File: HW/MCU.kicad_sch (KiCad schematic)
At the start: 44 parts, among them J4 UPDI Debug Connector, SW1 Reset, U2 ATmega4809-A, U4 24AA256UID

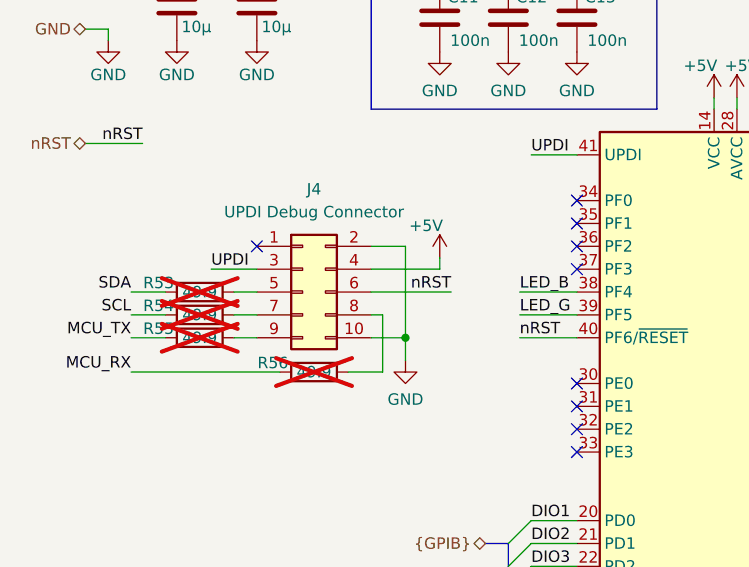
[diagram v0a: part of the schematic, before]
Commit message: Added uart and i2c to jtag connector, docs added
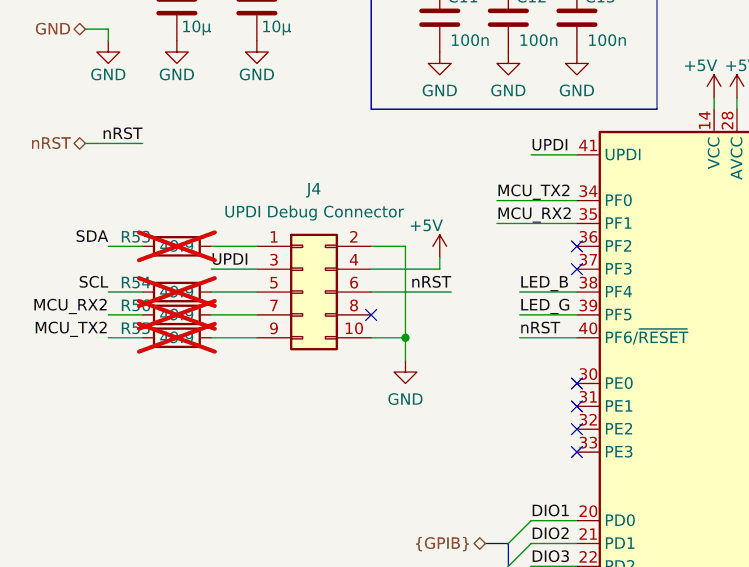
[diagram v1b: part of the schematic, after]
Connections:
- net MCU_RX: no longer R56.1
- net MCU_TX: no longer R55.1
- net at R56.2: now also J4.7 (Pin_7); no longer J4.8 (Pin_8)
- net at R54.2: now also J4.5 (Pin_5); no longer J4.7 (Pin_7)
- net at R53.2: now also J4.1 (Pin_1); no longer J4.5 (Pin_5)
- net MCU_TX2: now reaches U2.34 (PF0)
- net MCU_TX2: now also R55.1
- net MCU_RX2: now reaches U2.35 (PF1)
- net MCU_RX2: now also R56.1
- no-connect marks 9 -> 7
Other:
- moved on the sheet: R53, R54, R55, R56
